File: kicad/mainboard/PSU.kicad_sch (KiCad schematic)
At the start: 28 parts, among them J1 +12V BATTERY, J8 VDC INPUT, U11 7809TV, U12 7809TV, U13 7805TV, U5 LM2941T

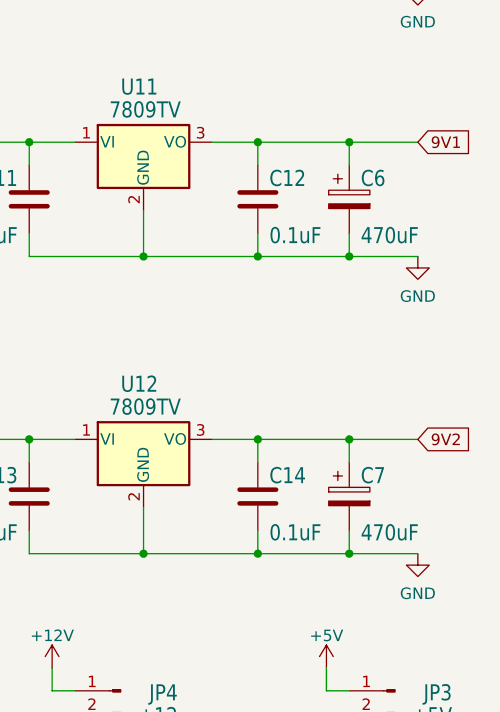
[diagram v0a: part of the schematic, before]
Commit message: Bringing mainboard up to par with V1.4 schematics based on images. Rerouted a few lines since they could not pass below the MOSFETs due to a different footprint/pad size.
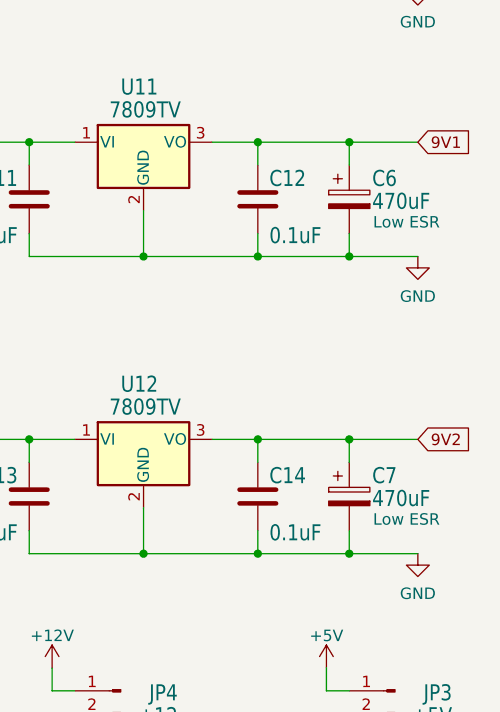
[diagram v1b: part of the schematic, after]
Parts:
- C6, C7: Comment (none) -> Low ESR
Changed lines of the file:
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@@
   (symbol (lib_id "Device:C_Polarized") (at 257.81 120.65 0) (unit 1)
     (in_bom yes) (on_board yes)
-    (property "Reference" "C7" (id 0) (at 259.08 119.38 0)
-      (effects (font (size 1.778 1.5113)) (justify left bottom))
-    )
-    (property "Value" "470uF" (id 1) (at 259.08 125.73 0)
+    (property "Reference" "C7" (id 0) (at 260.35 119.38 0)
+      (effects (font (size 1.778 1.5113)) (justify left bottom))
+    )
+    (property "Value" "470uF" (id 1) (at 260.35 121.92 0)
       (effects (font (size 1.778 1.5113)) (justify left bottom))
     )
@@
       (effects (font (size 1.27 1.27)) hide)
     )
+    (property "Comment" "Low ESR" (id 4) (at 264.16 123.19 0))
     (pin "1")
     (pin "2")
@@
   (symbol (lib_id "Device:C_Polarized") (at 257.81 87.63 0) (unit 1)
     (in_bom yes) (on_board yes)
-    (property "Reference" "C6" (id 0) (at 259.08 86.36 0)
-      (effects (font (size 1.778 1.5113)) (justify left bottom))
-    )
-    (property "Value" "470uF" (id 1) (at 259.08 92.71 0)
+    (property "Reference" "C6" (id 0) (at 260.35 86.36 0)
+      (effects (font (size 1.778 1.5113)) (justify left bottom))
+    )
+    (property "Value" "470uF" (id 1) (at 260.35 88.9 0)
       (effects (font (size 1.778 1.5113)) (justify left bottom))
     )
@@
       (effects (font (size 1.27 1.27)) hide)
     )
-    (pin "1")
-    (pin "2")
+    (property "Comment" "Low ESR" (id 4) (at 264.16 90.17 0))
+    (pin "1")
+    (pin "2")

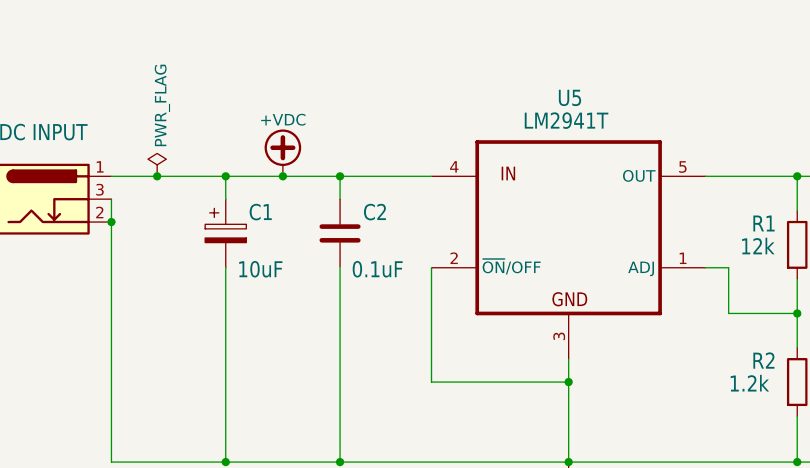
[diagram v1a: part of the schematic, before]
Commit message: Brought component numbers back in line with the original schematics
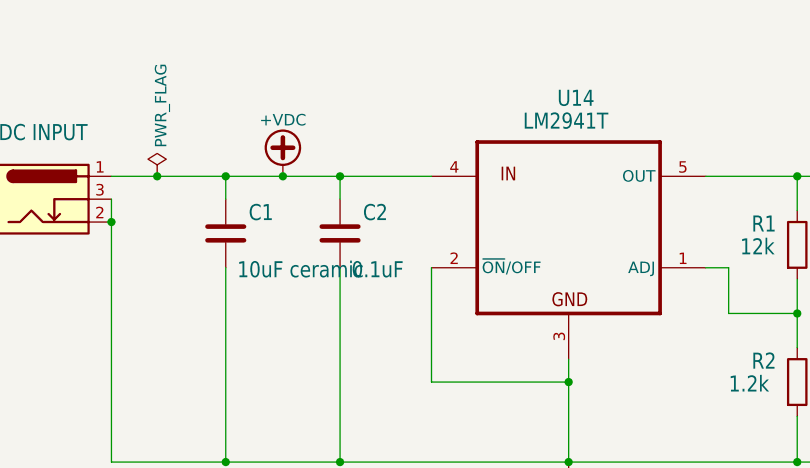
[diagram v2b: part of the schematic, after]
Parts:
- C1: value 10uF -> 10uF ceramic; footprint Capacitor_THT:CP_Radial_D6.3mm_P2.50mm -> Capacitor_THT:C_Disc_D5.0mm_W2.5mm_P2.50mm; symbol Device:C_Polarized -> Device:C; Comment (none) -> Ceramic
- renumbered U5 to U14
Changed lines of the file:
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@@
     (pin "1")
   )
-  (symbol (lib_id "Device:C_Polarized") (at 52.07 57.15 0) (unit 1)
+  (symbol (lib_id "Device:C") (at 52.07 57.15 0) (unit 1)
     (in_bom yes) (on_board yes)
     (property "Reference" "C1" (id 0) (at 54.61 55.88 0)
       (effects (font (size 1.778 1.5113)) (justify left bottom))
     )
-    (property "Value" "10uF" (id 1) (at 53.34 62.23 0)
+    (property "Value" "10uF ceramic" (id 1) (at 53.34 62.23 0)
       (effects (font (size 1.778 1.5113)) (justify left bottom))
     )
-    (property "Footprint" "Capacitor_THT:CP_Radial_D6.3mm_P2.50mm" (id 2) (at 53.0352 60.96 0)
+    (property "Footprint" "Capacitor_THT:C_Disc_D5.0mm_W2.5mm_P2.50mm" (id 2) (at 53.0352 60.96 0)
       (effects (font (size 1.27 1.27)) hide)
     )
     (property "Datasheet" "~" (id 3) (at 52.07 57.15 0)
+      (effects (font (size 1.27 1.27)) hide)
+    )
+    (property "Comment" "Ceramic" (id 4) (at 52.07 57.15 0)
       (effects (font (size 1.27 1.27)) hide)
     )
@@
   (symbol (lib_id "mk312-eagle-import:LM2941T") (at 90.17 55.88 0) (unit 1)
     (in_bom yes) (on_board yes)
-    (property "Reference" "U5" (id 0) (at 88.9 43.18 0)
+    (property "Reference" "U14" (id 0) (at 88.9 43.18 0)
       (effects (font (size 1.778 1.5113)) (justify left bottom))
     )

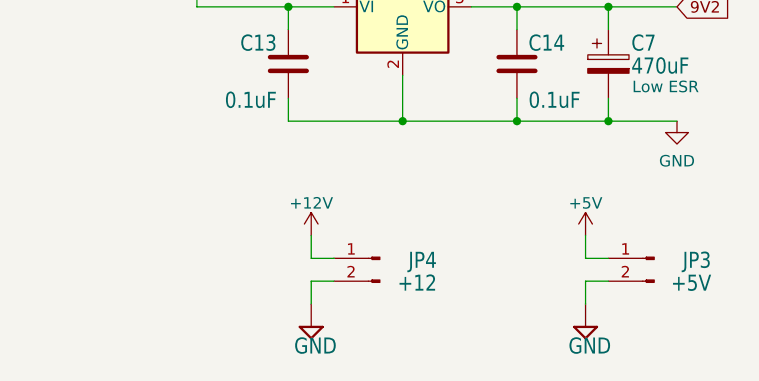
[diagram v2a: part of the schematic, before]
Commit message: Putting in new combined footprint for transformer. Updated F.Fab layer with component values in the correct place
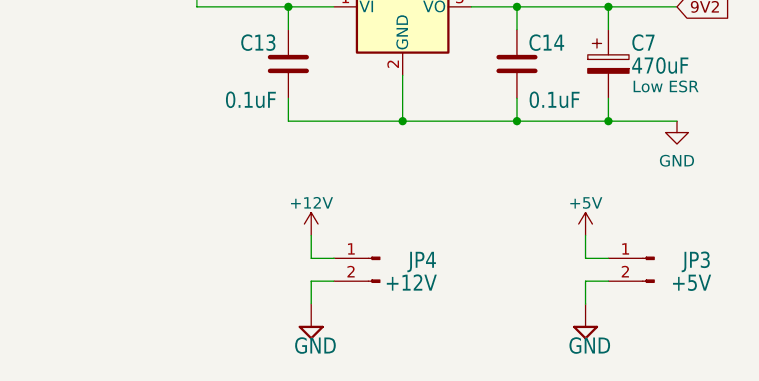
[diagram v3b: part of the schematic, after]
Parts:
- JP4: value +12 -> +12V
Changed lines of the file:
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@@
       (effects (font (size 1.778 1.5113)) (justify left bottom))
     )
-    (property "Value" "+12" (id 1) (at 238.76 146.05 0)
+    (property "Value" "+12V" (id 1) (at 238.76 146.05 0)
       (effects (font (size 1.778 1.5113)) (justify left bottom))
     )

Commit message: Fixed footprint for powerbus connector. Bumped version to 1.4.1.
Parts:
- J8: footprint Connector_BarrelJack:BarrelJack_CUI_PJ-102AH_Horizontal -> Connector_BarrelJack:BarrelJack_GCT_DCJ200-10-A_Horizontal
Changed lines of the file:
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@@
   (title_block
     (title "Power supply")
-    (date "2022-08-01")
-    (rev "1.3-Chi")
+    (date "2022-09-04")
+    (rev "1.4.1-chi")
   )
   (junction (at 39.37 55.88) (diameter 0) (color 0 0 0 0)
@@
       (effects (font (size 1.778 1.5113)) (justify left bottom))
     )
-    (property "Footprint" "Connector_BarrelJack:BarrelJack_CUI_PJ-102AH_Horizontal" (id 2) (at 33.02 54.356 0)
-      (effects (font (size 1.27 1.27)) hide)
-    )
+    (property "Footprint" "Connector_BarrelJack:BarrelJack_GCT_DCJ200-10-A_Horizontal" (id 2) (at 33.02 54.356 0)
+      (effects (font (size 1.27 1.27)) hide)
+    )
